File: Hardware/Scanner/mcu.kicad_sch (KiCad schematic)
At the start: 8 parts, among them Q1 BSS138DW-7-F, U6 AS7341-DLGT

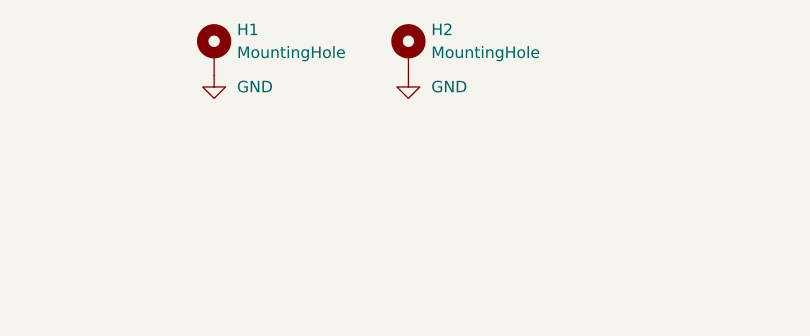
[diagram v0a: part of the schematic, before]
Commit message: Updated LED and crystal descriptions
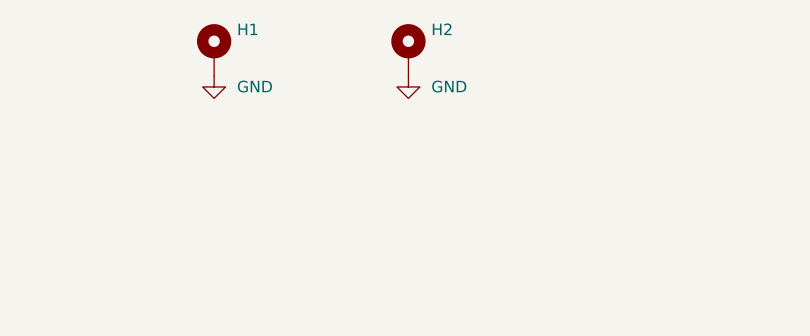
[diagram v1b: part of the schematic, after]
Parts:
- H1, H2: value MountingHole -> (none); footprint MountingHole:MountingHole_2.2mm_M2_ISO7380_Pad -> (none); now left out of the parts list
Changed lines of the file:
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@@
   )
   (symbol (lib_id "Mechanical:MountingHole_Pad") (at 204.47 31.75 0) (unit 1)
-    (in_bom yes) (on_board yes) (fields_autoplaced)
+    (in_bom no) (on_board yes) (fields_autoplaced)
     (property "Reference" "H2" (id 0) (at 207.01 29.2099 0)
       (effects (font (size 1.27 1.27)) (justify left))
     )
-    (property "Value" "MountingHole" (id 1) (at 207.01 31.7499 0)
-      (effects (font (size 1.27 1.27)) (justify left))
-    )
-    (property "Footprint" "MountingHole:MountingHole_2.2mm_M2_ISO7380_Pad" (id 2) (at 204.47 31.75 0)
+    (property "Value" "" (id 1) (at 207.01 31.7499 0)
+      (effects (font (size 1.27 1.27)) (justify left))
+    )
+    (property "Footprint" "" (id 2) (at 204.47 31.75 0)
       (effects (font (size 1.27 1.27)) hide)
     )
@@
   )
   (symbol (lib_id "Mechanical:MountingHole_Pad") (at 182.88 31.75 0) (unit 1)
-    (in_bom yes) (on_board yes) (fields_autoplaced)
+    (in_bom no) (on_board yes) (fields_autoplaced)
     (property "Reference" "H1" (id 0) (at 185.42 29.2099 0)
       (effects (font (size 1.27 1.27)) (justify left))
     )
-    (property "Value" "MountingHole" (id 1) (at 185.42 31.7499 0)
-      (effects (font (size 1.27 1.27)) (justify left))
-    )
-    (property "Footprint" "MountingHole:MountingHole_2.2mm_M2_ISO7380_Pad" (id 2) (at 182.88 31.75 0)
-      (effects (font (size 1.27 1.27)) hide)
-    )
+    (property "Value" "" (id 1) (at 185.42 31.7499 0)
+      (effects (font (size 1.27 1.27)) (justify left))
+    )
+    (property "Footprint" "" (id 2) (at 182.88 31.75 0)
+      (effects (font (size 1.27 1.27)) hide)
+    )

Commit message: Consistency of capacitor values
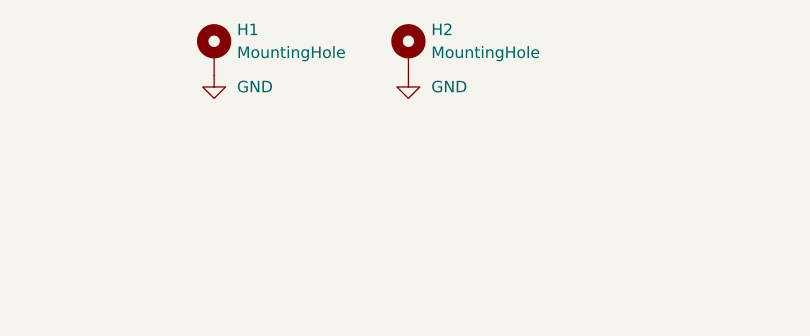
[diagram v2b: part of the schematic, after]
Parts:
- H1, H2: value (none) -> MountingHole; footprint (none) -> MountingHole:MountingHole_2.2mm_M2_ISO7380_Pad
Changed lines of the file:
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@@
       (effects (font (size 1.27 1.27)) (justify left))
     )
-    (property "Value" "" (id 1) (at 207.01 31.7499 0)
-      (effects (font (size 1.27 1.27)) (justify left))
-    )
-    (property "Footprint" "" (id 2) (at 204.47 31.75 0)
+    (property "Value" "MountingHole" (id 1) (at 207.01 31.7499 0)
+      (effects (font (size 1.27 1.27)) (justify left))
+    )
+    (property "Footprint" "MountingHole:MountingHole_2.2mm_M2_ISO7380_Pad" (id 2) (at 204.47 31.75 0)
       (effects (font (size 1.27 1.27)) hide)
     )
@@
       (effects (font (size 1.27 1.27)) (justify left))
     )
-    (property "Value" "" (id 1) (at 185.42 31.7499 0)
-      (effects (font (size 1.27 1.27)) (justify left))
-    )
-    (property "Footprint" "" (id 2) (at 182.88 31.75 0)
-      (effects (font (size 1.27 1.27)) hide)
-    )
+    (property "Value" "MountingHole" (id 1) (at 185.42 31.7499 0)
+      (effects (font (size 1.27 1.27)) (justify left))
+    )
+    (property "Footprint" "MountingHole:MountingHole_2.2mm_M2_ISO7380_Pad" (id 2) (at 182.88 31.75 0)
+      (effects (font (size 1.27 1.27)) hide)
+    )
